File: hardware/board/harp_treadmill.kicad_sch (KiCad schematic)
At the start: 12 parts

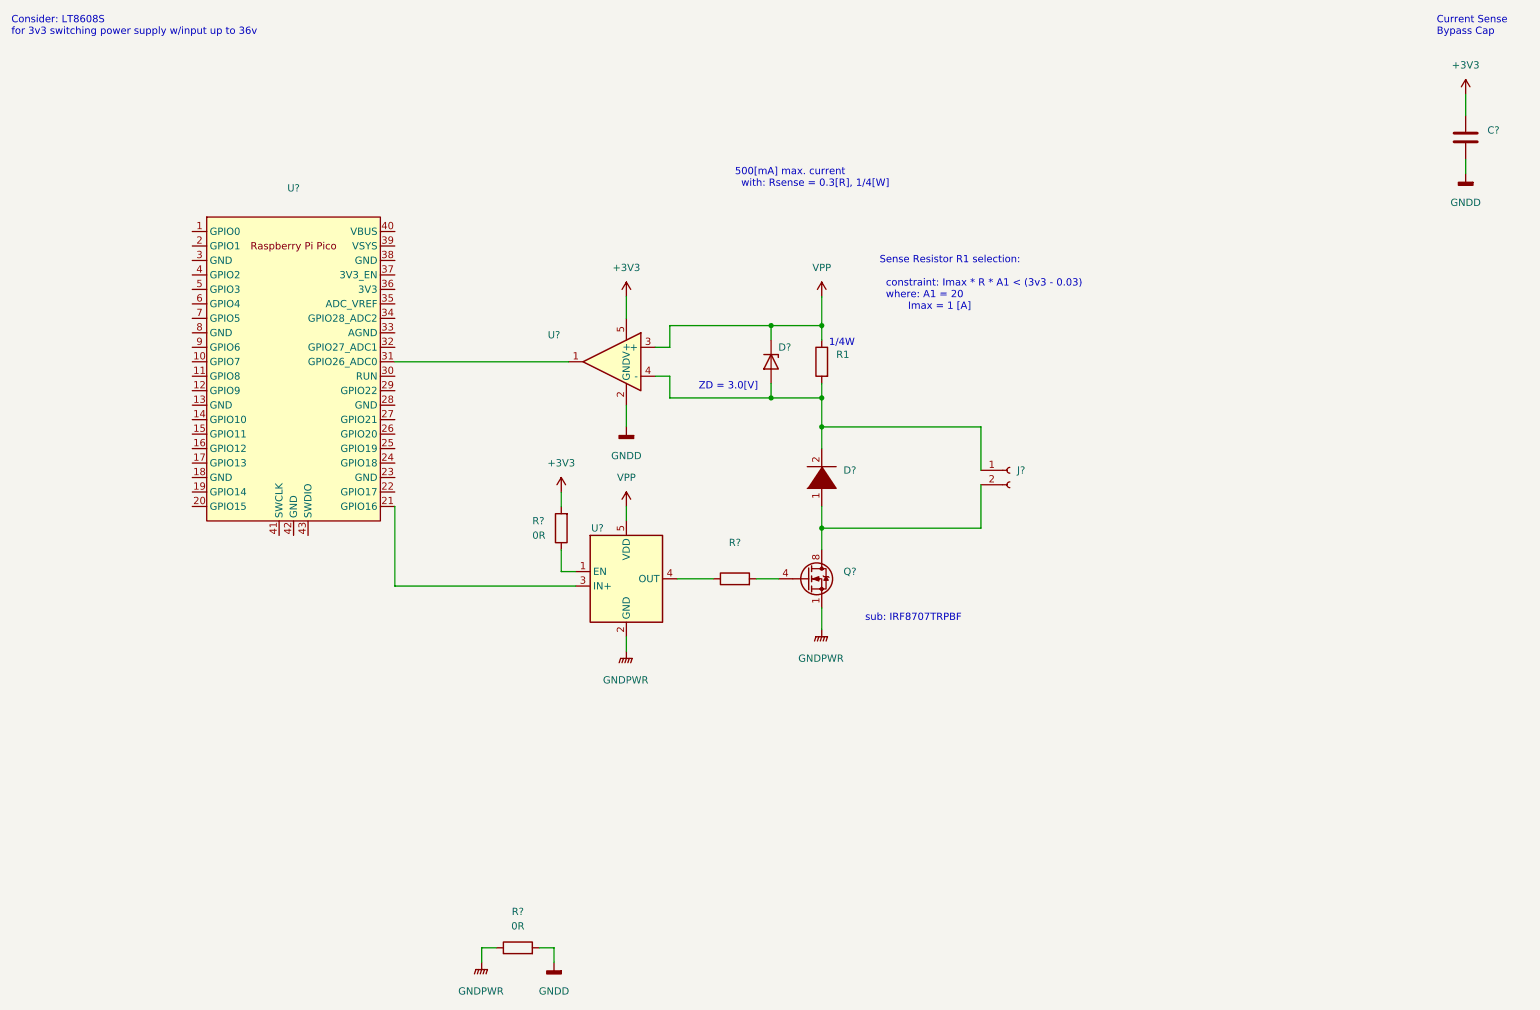
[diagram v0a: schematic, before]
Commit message: adc reading works
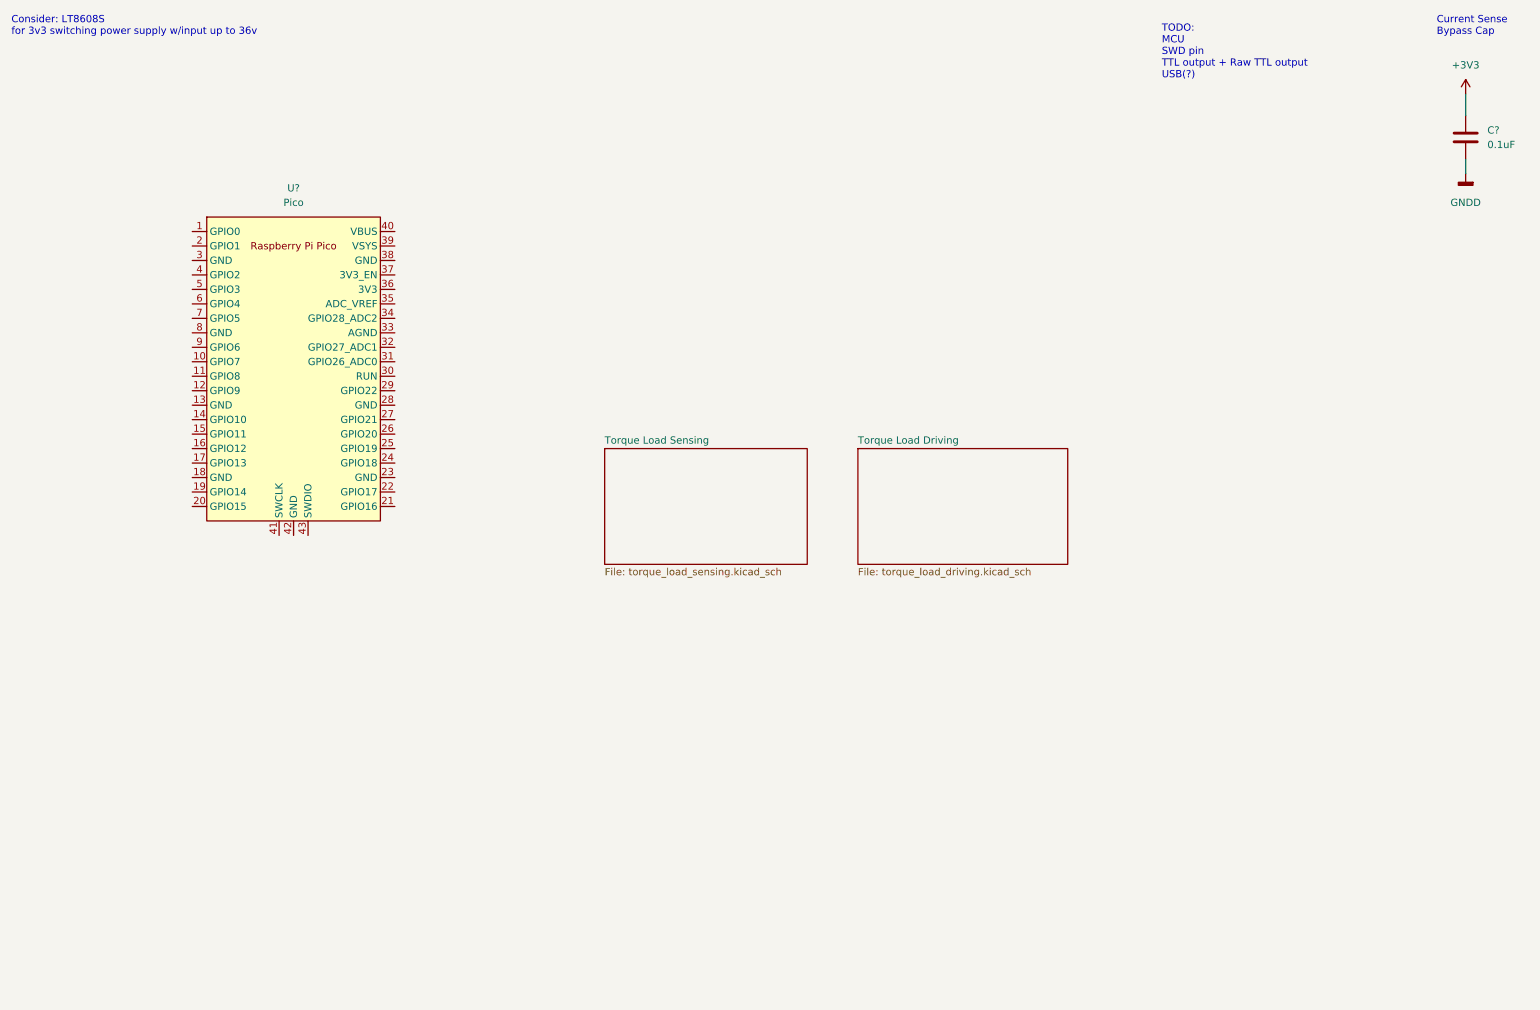
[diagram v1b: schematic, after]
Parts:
- removed D?: (no value), symbol Device:D_Zener
- removed D?: (no value), symbol pspice:DIODE
- removed J?: (no value), symbol Connector:Conn_01x02_Female
- removed Q?: (no value), symbol Transistor_FET:IRF7403
- removed R1, R?: (no value), symbol Device:R
- removed R? (x2): 0R, symbol Device:R
- removed U?: (no value), Package_TO_SOT_SMD:SOT-23-5, symbol machine_agency_components:UCC27537
- removed U?: (no value), symbol machine_agency_components:INA180
- C?: value (none) -> 0.1uF
- U?: value (none) -> Pico; footprint (none) -> RPi_Pico:RPi_Pico_SMD_TH
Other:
- added sheet Torque Load Driving (torque_load_driving.kicad_sch)
- added sheet Torque Load Sensing (torque_load_sensing.kicad_sch)
- note added: "TODO: MCU SWD pin TTL output + Raw TTL output USB(?)"
- note removed: "1/4W"
- note removed: "500[mA] max. current with: Rsense = 0.3[R], 1/4[W]"
- note removed: "Sense Resistor R1 selection: constraint: Imax * R * A1 < (3v3 - 0.03) where: A1 = 20 Imax = 1 [A]"
- note removed: "ZD = 3.0[V]"
- note removed: "sub: IRF8707TRPBF"

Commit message: update board schematic
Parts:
- removed U?: Pico, RPi_Pico:RPi_Pico_SMD_TH, symbol pi_pico:Pico
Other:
- note added: "TODO: power supplies for AFE TODO: power supply for brake. also brake part number. TODO: harp core rp2040 TODO: read INA180 datasheet section on filtering. ASK: TTL enable/disable? threshold?"
- note removed: "TODO: MCU SWD pin TTL output + Raw TTL output USB(?)"

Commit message: update pcb
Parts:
- removed C?: 0.1uF, symbol Device:C
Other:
- sheet Torque Load Driving renamed Magnetic Brake Control
- sheet Torque Load Sensing renamed Torque Transducer Sensing
- added sheet Encoder (encoder_5_to_3v3.kicad_sch)
- added sheet Harp Core RP2040 + Isolated USB (harp_core_rp2040_w_isolated_usb.kicad_sch)
- added sheet Power Supplies (power_supplies.kicad_sch)
- sheet Magnetic Brake Control ports: added ADC_CS, ADC_POCI, ADC_SCK; removed none
- sheet Torque Transducer Sensing ports: added ADC_CS, ADC_POCI, ADC_SCK; removed none
- note added: "TODO: power supplies for AFE TODO: power supply for brake. Needs to be fixed @12v. also brake part number. TODO: bypass caps for both ADS7049 chips and literally everything else. TODO: read INA180 datasheet section on filtering. DONE: TODO: harp core rp2040 DONE: encoder with 3.3-5V logic level translation."
- note removed: "Consider: LT8608S for 3v3 switching power supply w/input up to 36v"
- note removed: "Current Sense Bypass Cap"
- note removed: "TODO: power supplies for AFE TODO: power supply for brake. also brake part number. TODO: harp core rp2040 TODO: read INA180 datasheet section on filtering. ASK: TTL enable/disable? threshold?"

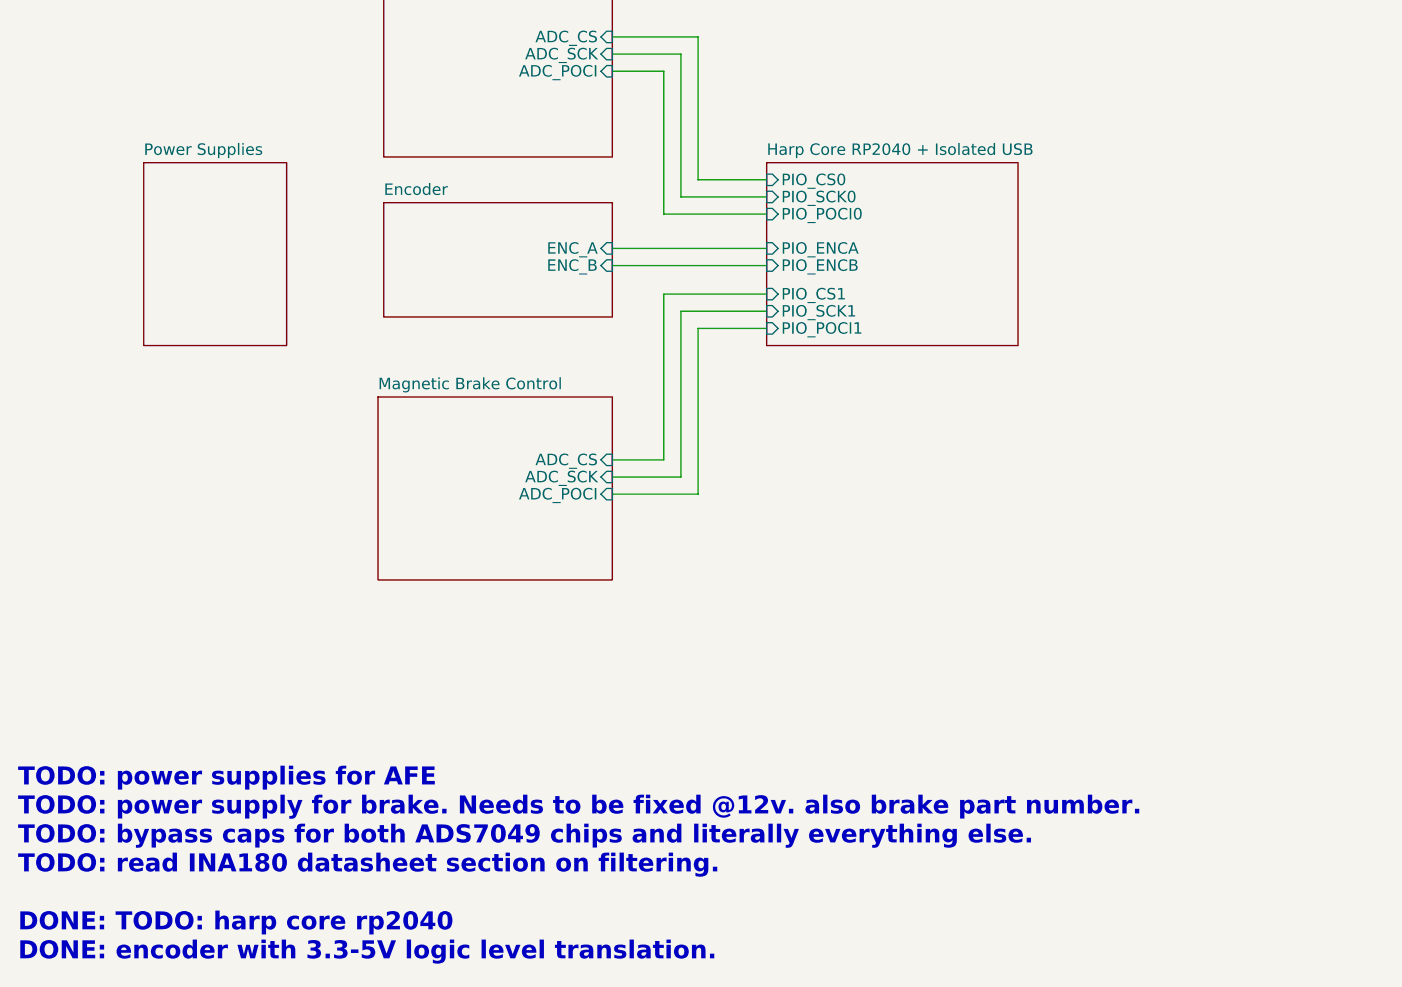
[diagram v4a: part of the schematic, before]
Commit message: update schematic
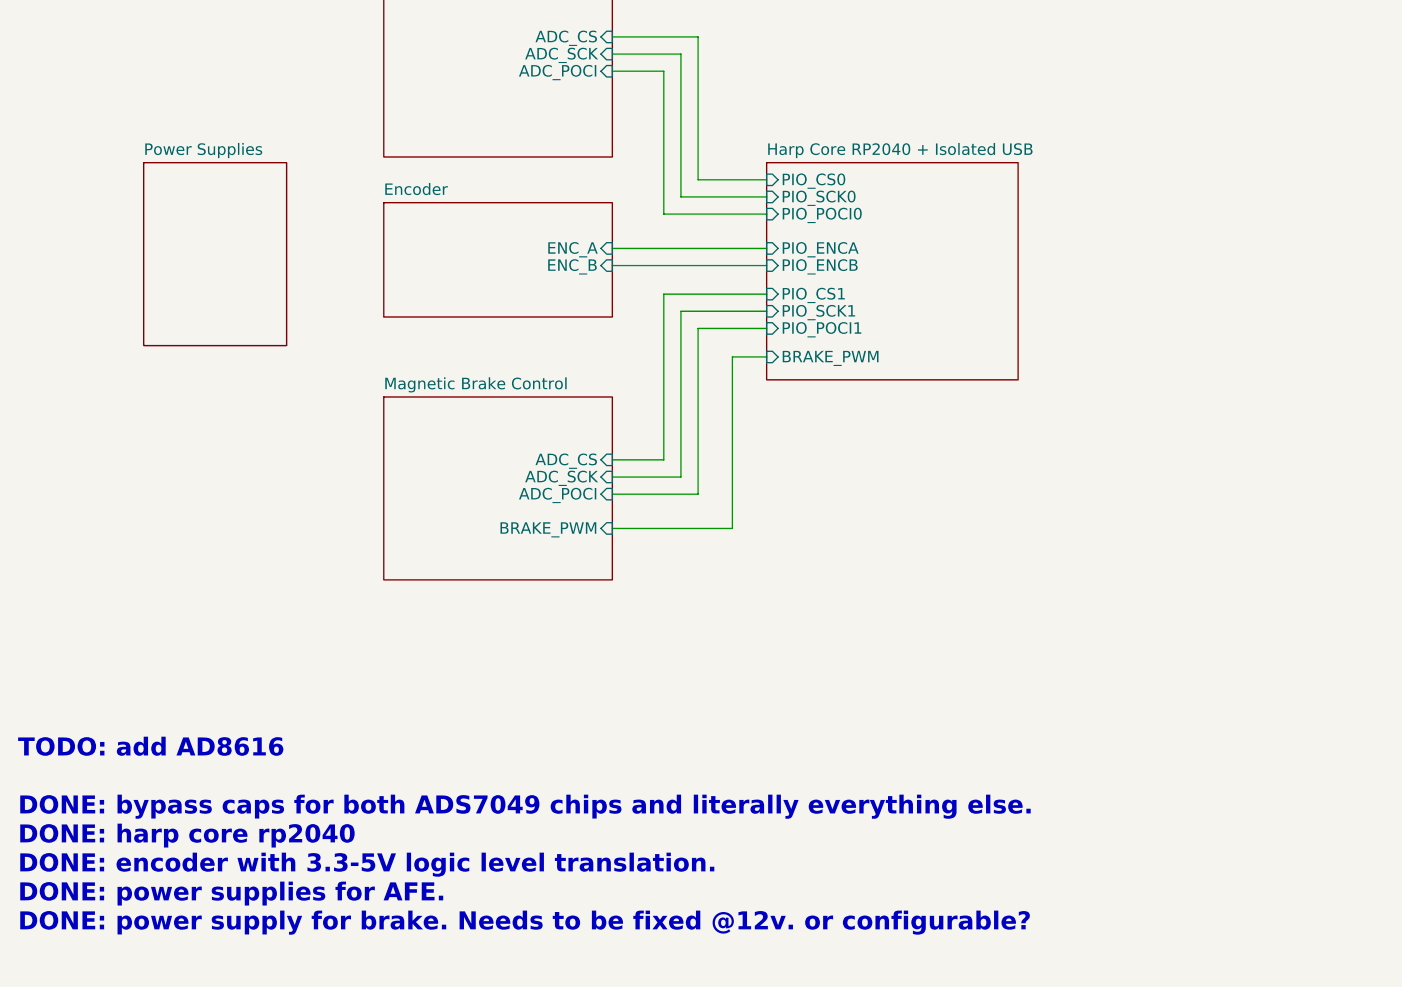
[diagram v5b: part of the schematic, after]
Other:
- sheet Harp Core RP2040 + Isolated USB ports: added BRAKE_PWM; removed none
- sheet Magnetic Brake Control ports: added BRAKE_PWM; removed none
- note added: "TODO: add AD8616 DONE: bypass caps for both ADS7049 chips and literally everything else. DONE: harp core rp2040 DONE: encoder with 3.3-5V logic level translation. DONE: power supplies for AFE. DONE: power supply for brake. Needs to be fixed @12v. or configurable?"
- note removed: "TODO: power supplies for AFE TODO: power supply for brake. Needs to be fixed @12v. also brake part number. TODO: bypass caps for both ADS7049 chips and literally everything else. TODO: read INA180 datasheet section on filtering. DONE: TODO: harp core rp2040 DONE: encoder with 3.3-5V logic level translation."
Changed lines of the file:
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@@
+    (stroke (width 0) (type default))
+  )
+  (wire (pts (xy 171.45 90.805) (xy 167.64 90.805))
     (stroke (width 0) (type default))
   )
@@
     (stroke (width 0) (type default))
   )
+  (wire (pts (xy 154.305 109.855) (xy 167.64 109.855))
+    (stroke (width 0) (type default))
+  )
   (wire (pts (xy 160.02 59.055) (xy 154.305 59.055))
     (stroke (width 0) (type default))
@@
     (stroke (width 0) (type default))
   )
-  (text "TODO: power supplies for AFE\nTODO: power supply for brake. Needs to be fixed @12v. also brake part number.\nTODO: bypass caps for both ADS7049 chips and literally everything else.\nTODO: read INA180 datasheet section on filtering.\n\nDONE: TODO: harp core rp2040\nDONE: encoder with 3.3-5V logic level translation.\n"
+  (wire (pts (xy 167.64 90.805) (xy 167.64 109.855))
+    (stroke (width 0) (type default))
+  )
+  (text "TODO: add AD8616\n\nDONE: bypass caps for both ADS7049 chips and literally everything else.\nDONE: harp core rp2040\nDONE: encoder with 3.3-5V logic level translation.\nDONE: power supplies for AFE.\nDONE: power supply for brake. Needs to be fixed @12v. or configurable?\n\n"
     (at 88.265 158.115 0)
     (effects (font (size 2 2) (thickness 0.4) bold) (justify left bottom))
@@
     )
   )
-  (sheet (at 128.27 95.25) (size 26.035 20.32) (fields_autoplaced)
+  (sheet (at 128.905 95.25) (size 25.4 20.32) (fields_autoplaced)
     (stroke (width 0.1524) (type solid))
     (fill (color 0 0 0 0.0000))
-    (property "Sheetname" "Magnetic Brake Control" (at 128.27 94.5384 0)
+    (property "Sheetname" "Magnetic Brake Control" (at 128.905 94.5384 0)
       (effects (font (size 1.27 1.27)) (justify left bottom))
     )
-    (property "Sheetfile" "torque_load_driving.kicad_sch" (at 128.27 116.1546 0)
+    (property "Sheetfile" "torque_load_driving.kicad_sch" (at 128.905 116.1546 0)
       (effects (font (size 1.27 1.27)) (justify left top) hide)
     )
@@
     )
     (pin "ADC_SCK" input (at 154.305 104.14 0)
+      (effects (font (size 1.27 1.27)) (justify right))
+    )
+    (pin "BRAKE_PWM" input (at 154.305 109.855 0)
       (effects (font (size 1.27 1.27)) (justify right))
     )
@@
     )
   )
-  (sheet (at 171.45 69.215) (size 27.94 20.32) (fields_autoplaced)
+  (sheet (at 171.45 69.215) (size 27.94 24.13) (fields_autoplaced)
     (stroke (width 0.1524) (type solid))
     (fill (color 0 0 0 0.0000))
@@
       (effects (font (size 1.27 1.27)) (justify left bottom))
     )
-    (property "Sheetfile" "harp_core_rp2040_w_isolated_usb.kicad_sch" (at 171.45 90.1196 0)
+    (property "Sheetfile" "harp_core_rp2040_w_isolated_usb.kicad_sch" (at 171.45 93.9296 0)
       (effects (font (size 1.27 1.27)) (justify left top) hide)
     )
@@
       (effects (font (size 1.27 1.27)) (justify left))
     )
+    (pin "BRAKE_PWM" input (at 171.45 90.805 180)
+      (effects (font (size 1.27 1.27)) (justify left))
+    )

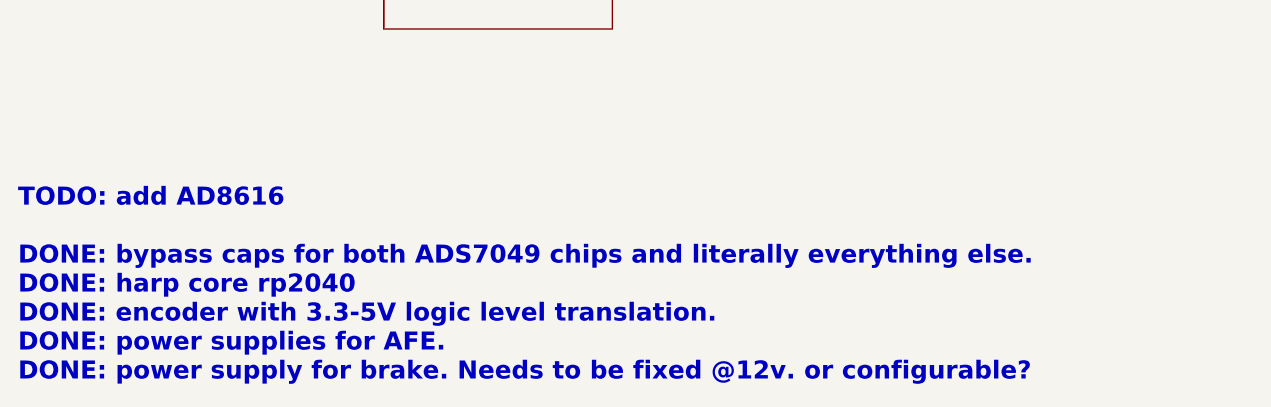
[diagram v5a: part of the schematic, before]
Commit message: update schematic
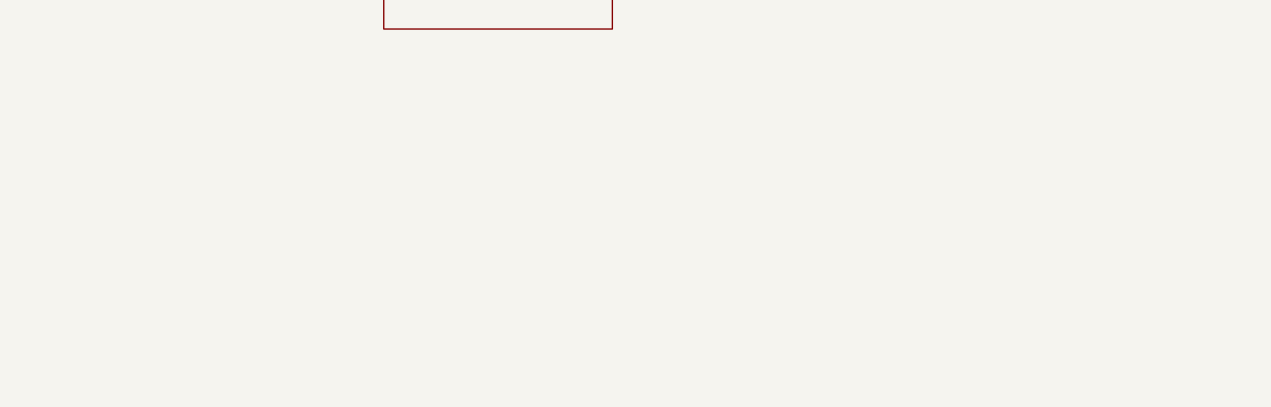
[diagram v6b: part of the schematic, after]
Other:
- note removed: "TODO: add AD8616 DONE: bypass caps for both ADS7049 chips and literally everything else. DONE: harp core rp2040 DONE: encoder with 3.3-5V logic level translation. DONE: power supplies for AFE. DONE: power supply for brake. Needs to be fixed @12v. or configurable?"
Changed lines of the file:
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@@
     (stroke (width 0) (type default))
-  )
-  (text "TODO: add AD8616\n\nDONE: bypass caps for both ADS7049 chips and literally everything else.\nDONE: harp core rp2040\nDONE: encoder with 3.3-5V logic level translation.\nDONE: power supplies for AFE.\nDONE: power supply for brake. Needs to be fixed @12v. or configurable?\n\n"
-    (at 88.265 158.115 0)
-    (effects (font (size 2 2) (thickness 0.4) bold) (justify left bottom))
   )
   (sheet (at 102.235 69.215) (size 15.875 20.32) (fields_autoplaced)

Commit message: update pcb
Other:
- note added: "FIXME: REF2033 bypass caps don't have footprints specified."
- note added: "TODO: consider 6V and 12V setting via resistors? We could buffer the feedback resistor value into the PICO's built-in ADC."
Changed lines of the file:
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@@
     (stroke (width 0) (type default))
+  )
+  (text "FIXME: REF2033 bypass caps don't have footprints specified."
+    (at 118.11 141.605 0)
+    (effects (font (face "KiCad Font") (size 2 2) (thickness 0.4) bold) (justify left bottom))
+  )
+  (text "TODO: consider 6V and 12V setting via resistors?\n    We could buffer the feedback resistor value into the\n    PICO's built-in ADC."
+    (at 118.11 130.81 0)
+    (effects (font (size 1.27 1.27)) (justify left bottom))
   )
   (sheet (at 102.235 69.215) (size 15.875 20.32) (fields_autoplaced)
